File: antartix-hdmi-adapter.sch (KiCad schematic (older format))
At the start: 17 parts

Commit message: Merge PCB design - Revision bumped to 1.1.0
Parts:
- added R?: R_0R_0805, antmicro-footprints:0805-res, symbol antmicroResistorsmisc:R_0R_0805
- gave numbers to parts that had none: 17
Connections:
- net labels added: 3V3_RPI
- wire segments 144 -> 145
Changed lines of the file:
@@
 Text GLabel 1650 3575 0    50   Input ~ 0
 HDMI0_CEC
-Text GLabel 1650 3775 0    50   Input ~ 0
-VCC3V3
 Text GLabel 2900 3575 2    50   Input ~ 0
 HDMI0_SDA
@@
 	2900 3675 2525 3675
 Wire Wire Line
-	1650 3775 2025 3775
-Wire Wire Line
 	2025 3775 2025 3875
 Wire Wire Line
@@
 	2275 4150 2275 4350
 $Comp
-L power:GND #PWR?
+L power:GND #PWR09
 U 1 1 6041C11F
 P 2275 4350
-F 0 "#PWR?" H 2275 4100 50  0001 C CNN
+F 0 "#PWR09" H 2275 4100 50  0001 C CNN
 F 1 "GND" H 2280 4177 50  0000 C CNN
 F 2 "" H 2275 4350 50  0001 C CNN
@@
 $EndComp
 $Comp
-L antmicroUSBDVIHDMIConnectors:685119134923 J?
+L antmicroUSBDVIHDMIConnectors:685119134923 J8
 U 1 1 6041EE42
 P 6700 2625
-F 0 "J?" H 6700 3562 60  0000 C CNN
+F 0 "J8" H 6700 3562 60  0000 C CNN
 F 1 "685119134923" H 6700 3456 60  0000 C CNN
 F 2 "antmicro-footprints:HDMI_A_Female_685119134923" H 6900 2825 60  0001 L CNN
@@
 	6400 3425 6400 3575
 $Comp
-L power:GND #PWR?
+L power:GND #PWR028
 U 1 1 6044467C
 P 6150 3575
-F 0 "#PWR?" H 6150 3325 50  0001 C CNN
+F 0 "#PWR028" H 6150 3325 50  0001 C CNN
 F 1 "GND" H 6155 3402 50  0000 C CNN
 F 2 "" H 6150 3575 50  0001 C CNN
@@
 $EndComp
 $Comp
-L power:GND #PWR?
+L power:GND #PWR031
 U 1 1 604461F7
 P 6400 3575
-F 0 "#PWR?" H 6400 3325 50  0001 C CNN
+F 0 "#PWR031" H 6400 3325 50  0001 C CNN
 F 1 "GND" H 6405 3402 50  0000 C CNN
 F 2 "" H 6400 3575 50  0001 C CNN
@@
 $EndComp
 $Comp
-L power:GND #PWR?
+L power:GND #PWR032
 U 1 1 604480F0
 P 7275 3575
-F 0 "#PWR?" H 7275 3325 50  0001 C CNN
+F 0 "#PWR032" H 7275 3325 50  0001 C CNN
 F 1 "GND" H 7280 3402 50  0000 C CNN
 F 2 "" H 7275 3575 50  0001 C CNN
@@
 HDMI0_CK_N
 $Comp
-L antmicroTVSDiodes:TPD8S009DSMR IC?
+L antmicroTVSDiodes:TPD8S009DSMR IC2
 U 1 1 60462849
 P 7675 4825
-F 0 "IC?" H 7700 5340 50  0000 C CNN
+F 0 "IC2" H 7700 5340 50  0000 C CNN
 F 1 "TPD8S009DSMR" H 7700 5249 50  0000 C CNN
 F 2 "antmicro-footprints:R-PDSO-N15" H 9075 4475 50  0001 C CNN
@@
 $EndComp
 $Comp
-L antmicroTestPoints:TP_SMD1MM TP?
+L antmicroTestPoints:TP_SMD1MM TP1
 U 1 1 60472FDB
 P 5500 2775
-F 0 "TP?" V 5405 2822 50  0000 C CNN
+F 0 "TP1" V 5405 2822 50  0000 C CNN
 F 1 "TP_SMD1MM" H 5500 2675 50  0001 C CNN
 F 2 "antmicro-footprints:Testpoint_smd_1mm" H 5700 2975 60  0001 L CNN
@@
 $EndComp
 $Comp
-L antmicroTestPoints:TP_SMD1MM TP?
+L antmicroTestPoints:TP_SMD1MM TP2
 U 1 1 604734EB
 P 5500 2875
-F 0 "TP?" V 5405 2922 50  0000 C CNN
+F 0 "TP2" V 5405 2922 50  0000 C CNN
 F 1 "TP_SMD1MM" H 5500 2775 50  0001 C CNN
 F 2 "antmicro-footprints:Testpoint_smd_1mm" H 5700 3075 60  0001 L CNN
@@
 $EndComp
 $Comp
-L antmicroTestPoints:TP_SMD1MM TP?
+L antmicroTestPoints:TP_SMD1MM TP3
 U 1 1 604737A0
 P 5500 3075
-F 0 "TP?" V 5405 3122 50  0000 C CNN
+F 0 "TP3" V 5405 3122 50  0000 C CNN
 F 1 "TP_SMD1MM" H 5500 2975 50  0001 C CNN
 F 2 "antmicro-footprints:Testpoint_smd_1mm" H 5700 3275 60  0001 L CNN
@@
 $EndComp
 $Comp
-L antmicroTestPoints:TP_SMD1MM TP?
+L antmicroTestPoints:TP_SMD1MM TP4
 U 1 1 60474952
 P 7900 2925
-F 0 "TP?" V 7900 2875 50  0000 R CNN
+F 0 "TP4" V 7900 2875 50  0000 R CNN
 F 1 "TP_SMD1MM" H 7900 2825 50  0001 C CNN
 F 2 "antmicro-footprints:Testpoint_smd_1mm" H 8100 3125 60  0001 L CNN
@@
 $EndComp
 $Comp
-L antmicroTestPoints:TP_SMD1MM TP?
+L antmicroTestPoints:TP_SMD1MM TP5
 U 1 1 60475CA9
 P 7900 3025
-F 0 "TP?" V 7900 2975 50  0000 R CNN
+F 0 "TP5" V 7900 2975 50  0000 R CNN
 F 1 "TP_SMD1MM" H 7900 2925 50  0001 C CNN
 F 2 "antmicro-footprints:Testpoint_smd_1mm" H 8100 3225 60  0001 L CNN
@@
 HDMI0_D2_P
 $Comp
-L power:GND #PWR?
+L power:GND #PWR033
 U 1 1 604E1D01
 P 7275 5950
-F 0 "#PWR?" H 7275 5700 50  0001 C CNN
+F 0 "#PWR033" H 7275 5700 50  0001 C CNN
 F 1 "GND" H 7280 5777 50  0000 C CNN
 F 2 "" H 7275 5950 50  0001 C CNN
@@
 $EndComp
 $Comp
-L antmicroUSBDVIHDMIConnectors:685119134923 J?
+L antmicroUSBDVIHDMIConnectors:685119134923 J9
 U 1 1 604E9CC4
 P 10450 2625
-F 0 "J?" H 10450 3562 60  0000 C CNN
+F 0 "J9" H 10450 3562 60  0000 C CNN
 F 1 "685119134923" H 10450 3456 60  0000 C CNN
 F 2 "antmicro-footprints:HDMI_A_Female_685119134923" H 10650 2825 60  0001 L CNN
@@
 	10150 3425 10150 3575
 $Comp
-L power:GND #PWR?
+L power:GND #PWR034
 U 1 1 604E9CE6
 P 9900 3575
-F 0 "#PWR?" H 9900 3325 50  0001 C CNN
+F 0 "#PWR034" H 9900 3325 50  0001 C CNN
 F 1 "GND" H 9905 3402 50  0000 C CNN
 F 2 "" H 9900 3575 50  0001 C CNN
@@
 $EndComp
 $Comp
-L power:GND #PWR?
+L power:GND #PWR035
 U 1 1 604E9CEC
 P 10150 3575
-F 0 "#PWR?" H 10150 3325 50  0001 C CNN
+F 0 "#PWR035" H 10150 3325 50  0001 C CNN
 F 1 "GND" H 10155 3402 50  0000 C CNN
 F 2 "" H 10150 3575 50  0001 C CNN
@@
 $EndComp
 $Comp
-L power:GND #PWR?
+L power:GND #PWR036
 U 1 1 604E9CF2
 P 11025 3575
-F 0 "#PWR?" H 11025 3325 50  0001 C CNN
+F 0 "#PWR036" H 11025 3325 50  0001 C CNN
 F 1 "GND" H 11030 3402 50  0000 C CNN
 F 2 "" H 11025 3575 50  0001 C CNN
@@
 HDMI1_CK_N
 $Comp
-L antmicroTVSDiodes:TPD8S009DSMR IC?
+L antmicroTVSDiodes:TPD8S009DSMR IC3
 U 1 1 604E9D00
 P 11425 4825
-F 0 "IC?" H 11450 5340 50  0000 C CNN
+F 0 "IC3" H 11450 5340 50  0000 C CNN
 F 1 "TPD8S009DSMR" H 11450 5249 50  0000 C CNN
 F 2 "antmicro-footprints:R-PDSO-N15" H 12825 4475 50  0001 C CNN
@@
 $EndComp
 $Comp
-L antmicroTestPoints:TP_SMD1MM TP?
+L antmicroTestPoints:TP_SMD1MM TP6
 U 1 1 604E9D06
 P 9250 2775
-F 0 "TP?" V 9155 2822 50  0000 C CNN
+F 0 "TP6" V 9155 2822 50  0000 C CNN
 F 1 "TP_SMD1MM" H 9250 2675 50  0001 C CNN
 F 2 "antmicro-footprints:Testpoint_smd_1mm" H 9450 2975 60  0001 L CNN
@@
 $EndComp
 $Comp
-L antmicroTestPoints:TP_SMD1MM TP?
+L antmicroTestPoints:TP_SMD1MM TP7
 U 1 1 604E9D0C
 P 9250 2875
-F 0 "TP?" V 9155 2922 50  0000 C CNN
+F 0 "TP7" V 9155 2922 50  0000 C CNN
 F 1 "TP_SMD1MM" H 9250 2775 50  0001 C CNN
 F 2 "antmicro-footprints:Testpoint_smd_1mm" H 9450 3075 60  0001 L CNN
@@
 $EndComp
 $Comp
-L antmicroTestPoints:TP_SMD1MM TP?
+L antmicroTestPoints:TP_SMD1MM TP8
 U 1 1 604E9D12
 P 9250 3075
-F 0 "TP?" V 9155 3122 50  0000 C CNN
+F 0 "TP8" V 9155 3122 50  0000 C CNN
 F 1 "TP_SMD1MM" H 9250 2975 50  0001 C CNN
 F 2 "antmicro-footprints:Testpoint_smd_1mm" H 9450 3275 60  0001 L CNN
@@
 $EndComp
 $Comp
-L antmicroTestPoints:TP_SMD1MM TP?
+L antmicroTestPoints:TP_SMD1MM TP9
 U 1 1 604E9D18
 P 11650 2925
-F 0 "TP?" V 11650 2875 50  0000 R CNN
+F 0 "TP9" V 11650 2875 50  0000 R CNN
 F 1 "TP_SMD1MM" H 11650 2825 50  0001 C CNN
 F 2 "antmicro-footprints:Testpoint_smd_1mm" H 11850 3125 60  0001 L CNN
@@
 $EndComp
 $Comp
-L antmicroTestPoints:TP_SMD1MM TP?
+L antmicroTestPoints:TP_SMD1MM TP10
 U 1 1 604E9D1E
 P 11650 3025
-F 0 "TP?" V 11650 2975 50  0000 R CNN
+F 0 "TP10" V 11650 2975 50  0000 R CNN
 F 1 "TP_SMD1MM" H 11650 2925 50  0001 C CNN
 F 2 "antmicro-footprints:Testpoint_smd_1mm" H 11850 3225 60  0001 L CNN
@@
 HDMI1_D2_P
 $Comp
-L power:GND #PWR?
+L power:GND #PWR037
 U 1 1 604E9D47
 P 11025 5950
-F 0 "#PWR?" H 11025 5700 50  0001 C CNN
+F 0 "#PWR037" H 11025 5700 50  0001 C CNN
 F 1 "GND" H 11030 5777 50  0000 C CNN
 F 2 "" H 11025 5950 50  0001 C CNN
@@
 	6300 2575 5600 2575
 $Comp
-L antmicroMechanicalParts:9774030151 SP?
+L antmicroMechanicalParts:9774030151 SP1
 U 1 1 603A356D
 P 13850 2400
-F 0 "SP?" H 13980 2453 60  0000 L CNN
+F 0 "SP1" H 13980 2453 60  0000 L CNN
 F 1 "9774030151" H 13980 2347 60  0000 L CNN
 F 2 "antmicro-footprints:9774030151" H 13850 2400 60  0001 C CNN
@@
 $EndComp
 $Comp
-L antmicroMechanicalParts:9774030151 SP?
+L antmicroMechanicalParts:9774030151 SP2
 U 1 1 603A4646
 P 13850 2775
-F 0 "SP?" H 13980 2828 60  0000 L CNN
+F 0 "SP2" H 13980 2828 60  0000 L CNN
 F 1 "9774030151" H 13980 2722 60  0000 L CNN
 F 2 "antmicro-footprints:9774030151" H 13850 2775 60  0001 C CNN
@@
 $EndComp
 $Comp
-L antmicroRectangularConnectorsHeadersFemalePins:QTE-020-04-L-D-A J?
+L antmicroRectangularConnectorsHeadersFemalePins:QTE-020-04-L-D-A J7
 U 1 1 60358E48
 P 2125 1925
-F 0 "J?" H 2275 2100 50  0000 C CNN
+F 0 "J7" H 2275 2100 50  0000 C CNN
 F 1 "QTE-020-04-L-D-A" H 2275 2009 50  0000 C CNN
 F 2 "antmicro-footprints:QTE-020-04-L-D-A" H 2275 -425 60  0001 L CNN
@@
 $EndComp
 Connection ~ 2025 3775
+Text Label 1325 3775 0    50   ~ 0
+3V3_RPI
+$Comp
+L antmicroResistorsmisc:R_0R_0805 R?
+U 1 1 6051B344
+P 1175 3775
+AR Path="/6051B344" Ref="R?"  Part="1"
+AR Path="/604C47E1/6051B344" Ref="R?"  Part="1"
+F 0 "R?" H 1050 3875 60  0000 C CNN
+F 1 "R_0R_0805" H 1175 3625 60  0001 C CNN
+F 2 "antmicro-footprints:0805-res" H 1375 3975 60  0001 L CNN
+F 3 "" H 1175 3775 50  0001 C CNN
+F 4 "VISHAY" H 1375 4175 60  0001 L CNN "Manufacturer"
+F 5 "CRCW08050000Z0EA" H 1375 4075 60  0001 L CNN "MPN"
+F 6 "0R" H 1175 3875 50  0000 C CNN "Val"
+F 7 "DNP" H 1175 3775 50  0000 C CNN "Populate"
+	1    1175 3775
+	1    0    0    -1
+$EndComp
+Text Label 1325 3775 0    50   ~ 0
+3V3_RPI
+Wire Wire Line
+	1325 3775 2025 3775
+Text GLabel 950  3775 0    50   Input ~ 0
+VCC3V3
+Wire Wire Line
+	1025 3775 950  3775
 $EndSCHEMATC

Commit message: Add hierarchical structure
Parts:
- gave numbers to parts that had none: 1
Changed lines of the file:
@@
 $Descr A3 16535 11693
 encoding utf-8
-Sheet 2 2
+Sheet 2 3
 Title ""
 Date ""
@@
 	2275 4150 2275 4350
 $Comp
-L power:GND #PWR09
+L power:GND #PWR068
 U 1 1 6041C11F
 P 2275 4350
-F 0 "#PWR09" H 2275 4100 50  0001 C CNN
+AR Path="/604C47E1/6041C11F" Ref="#PWR068"  Part="1"
+AR Path="/60603DE8/6041C11F" Ref="#PWR?"  Part="1"
+F 0 "#PWR068" H 2275 4100 50  0001 C CNN
 F 1 "GND" H 2280 4177 50  0000 C CNN
 F 2 "" H 2275 4350 50  0001 C CNN
@@
 U 1 1 6041EE42
 P 6700 2625
+AR Path="/604C47E1/6041EE42" Ref="J8"  Part="1"
+AR Path="/60603DE8/6041EE42" Ref="J?"  Part="1"
 F 0 "J8" H 6700 3562 60  0000 C CNN
 F 1 "685119134923" H 6700 3456 60  0000 C CNN
@@
 	6400 3425 6400 3575
 $Comp
-L power:GND #PWR028
+L power:GND #PWR069
 U 1 1 6044467C
 P 6150 3575
-F 0 "#PWR028" H 6150 3325 50  0001 C CNN
+AR Path="/604C47E1/6044467C" Ref="#PWR069"  Part="1"
+AR Path="/60603DE8/6044467C" Ref="#PWR?"  Part="1"
+F 0 "#PWR069" H 6150 3325 50  0001 C CNN
 F 1 "GND" H 6155 3402 50  0000 C CNN
 F 2 "" H 6150 3575 50  0001 C CNN
@@
 $EndComp
 $Comp
-L power:GND #PWR031
+L power:GND #PWR070
 U 1 1 604461F7
 P 6400 3575
-F 0 "#PWR031" H 6400 3325 50  0001 C CNN
+AR Path="/604C47E1/604461F7" Ref="#PWR070"  Part="1"
+AR Path="/60603DE8/604461F7" Ref="#PWR?"  Part="1"
+F 0 "#PWR070" H 6400 3325 50  0001 C CNN
 F 1 "GND" H 6405 3402 50  0000 C CNN
 F 2 "" H 6400 3575 50  0001 C CNN
@@
 $EndComp
 $Comp
-L power:GND #PWR032
+L power:GND #PWR071
 U 1 1 604480F0
 P 7275 3575
-F 0 "#PWR032" H 7275 3325 50  0001 C CNN
+AR Path="/604C47E1/604480F0" Ref="#PWR071"  Part="1"
+AR Path="/60603DE8/604480F0" Ref="#PWR?"  Part="1"
+F 0 "#PWR071" H 7275 3325 50  0001 C CNN
 F 1 "GND" H 7280 3402 50  0000 C CNN
 F 2 "" H 7275 3575 50  0001 C CNN
@@
 U 1 1 60462849
 P 7675 4825
+AR Path="/604C47E1/60462849" Ref="IC2"  Part="1"
+AR Path="/60603DE8/60462849" Ref="IC?"  Part="1"
 F 0 "IC2" H 7700 5340 50  0000 C CNN
 F 1 "TPD8S009DSMR" H 7700 5249 50  0000 C CNN
@@
 U 1 1 60472FDB
 P 5500 2775
+AR Path="/604C47E1/60472FDB" Ref="TP1"  Part="1"
+AR Path="/60603DE8/60472FDB" Ref="TP?"  Part="1"
 F 0 "TP1" V 5405 2822 50  0000 C CNN
 F 1 "TP_SMD1MM" H 5500 2675 50  0001 C CNN
@@
 U 1 1 604734EB
 P 5500 2875
+AR Path="/604C47E1/604734EB" Ref="TP2"  Part="1"
+AR Path="/60603DE8/604734EB" Ref="TP?"  Part="1"
 F 0 "TP2" V 5405 2922 50  0000 C CNN
 F 1 "TP_SMD1MM" H 5500 2775 50  0001 C CNN
@@
 U 1 1 604737A0
 P 5500 3075
+AR Path="/604C47E1/604737A0" Ref="TP3"  Part="1"
+AR Path="/60603DE8/604737A0" Ref="TP?"  Part="1"
 F 0 "TP3" V 5405 3122 50  0000 C CNN
 F 1 "TP_SMD1MM" H 5500 2975 50  0001 C CNN
@@
 U 1 1 60474952
 P 7900 2925
+AR Path="/604C47E1/60474952" Ref="TP4"  Part="1"
+AR Path="/60603DE8/60474952" Ref="TP?"  Part="1"
 F 0 "TP4" V 7900 2875 50  0000 R CNN
 F 1 "TP_SMD1MM" H 7900 2825 50  0001 C CNN
@@
 U 1 1 60475CA9
 P 7900 3025
+AR Path="/604C47E1/60475CA9" Ref="TP5"  Part="1"
+AR Path="/60603DE8/60475CA9" Ref="TP?"  Part="1"
 F 0 "TP5" V 7900 2975 50  0000 R CNN
 F 1 "TP_SMD1MM" H 7900 2925 50  0001 C CNN
@@
 HDMI0_D2_P
 $Comp
-L power:GND #PWR033
+L power:GND #PWR072
 U 1 1 604E1D01
 P 7275 5950
-F 0 "#PWR033" H 7275 5700 50  0001 C CNN
+AR Path="/604C47E1/604E1D01" Ref="#PWR072"  Part="1"
+AR Path="/60603DE8/604E1D01" Ref="#PWR?"  Part="1"
+F 0 "#PWR072" H 7275 5700 50  0001 C CNN
 F 1 "GND" H 7280 5777 50  0000 C CNN
 F 2 "" H 7275 5950 50  0001 C CNN
@@
 U 1 1 604E9CC4
 P 10450 2625
+AR Path="/604C47E1/604E9CC4" Ref="J9"  Part="1"
+AR Path="/60603DE8/604E9CC4" Ref="J?"  Part="1"
 F 0 "J9" H 10450 3562 60  0000 C CNN
 F 1 "685119134923" H 10450 3456 60  0000 C CNN
@@
 	10150 3425 10150 3575
 $Comp
-L power:GND #PWR034
+L power:GND #PWR073
 U 1 1 604E9CE6
 P 9900 3575
-F 0 "#PWR034" H 9900 3325 50  0001 C CNN
+AR Path="/604C47E1/604E9CE6" Ref="#PWR073"  Part="1"
+AR Path="/60603DE8/604E9CE6" Ref="#PWR?"  Part="1"
+F 0 "#PWR073" H 9900 3325 50  0001 C CNN
 F 1 "GND" H 9905 3402 50  0000 C CNN
 F 2 "" H 9900 3575 50  0001 C CNN
@@
 $EndComp
 $Comp
-L power:GND #PWR035
+L power:GND #PWR074
 U 1 1 604E9CEC
 P 10150 3575
-F 0 "#PWR035" H 10150 3325 50  0001 C CNN
+AR Path="/604C47E1/604E9CEC" Ref="#PWR074"  Part="1"
+AR Path="/60603DE8/604E9CEC" Ref="#PWR?"  Part="1"
+F 0 "#PWR074" H 10150 3325 50  0001 C CNN
 F 1 "GND" H 10155 3402 50  0000 C CNN
 F 2 "" H 10150 3575 50  0001 C CNN
@@
 $EndComp
 $Comp
-L power:GND #PWR036
+L power:GND #PWR075
 U 1 1 604E9CF2
 P 11025 3575
-F 0 "#PWR036" H 11025 3325 50  0001 C CNN
+AR Path="/604C47E1/604E9CF2" Ref="#PWR075"  Part="1"
+AR Path="/60603DE8/604E9CF2" Ref="#PWR?"  Part="1"
+F 0 "#PWR075" H 11025 3325 50  0001 C CNN
 F 1 "GND" H 11030 3402 50  0000 C CNN
 F 2 "" H 11025 3575 50  0001 C CNN
@@
 U 1 1 604E9D00
 P 11425 4825
+AR Path="/604C47E1/604E9D00" Ref="IC3"  Part="1"
+AR Path="/60603DE8/604E9D00" Ref="IC?"  Part="1"
 F 0 "IC3" H 11450 5340 50  0000 C CNN
 F 1 "TPD8S009DSMR" H 11450 5249 50  0000 C CNN
@@
 U 1 1 604E9D06
 P 9250 2775
+AR Path="/604C47E1/604E9D06" Ref="TP6"  Part="1"
+AR Path="/60603DE8/604E9D06" Ref="TP?"  Part="1"
 F 0 "TP6" V 9155 2822 50  0000 C CNN
 F 1 "TP_SMD1MM" H 9250 2675 50  0001 C CNN
@@
 U 1 1 604E9D0C
 P 9250 2875
+AR Path="/604C47E1/604E9D0C" Ref="TP7"  Part="1"
+AR Path="/60603DE8/604E9D0C" Ref="TP?"  Part="1"
 F 0 "TP7" V 9155 2922 50  0000 C CNN
 F 1 "TP_SMD1MM" H 9250 2775 50  0001 C CNN
@@
 U 1 1 604E9D12
 P 9250 3075
+AR Path="/604C47E1/604E9D12" Ref="TP8"  Part="1"
+AR Path="/60603DE8/604E9D12" Ref="TP?"  Part="1"
 F 0 "TP8" V 9155 3122 50  0000 C CNN
 F 1 "TP_SMD1MM" H 9250 2975 50  0001 C CNN
@@
 U 1 1 604E9D18
 P 11650 2925
+AR Path="/604C47E1/604E9D18" Ref="TP9"  Part="1"
+AR Path="/60603DE8/604E9D18" Ref="TP?"  Part="1"
 F 0 "TP9" V 11650 2875 50  0000 R CNN
 F 1 "TP_SMD1MM" H 11650 2825 50  0001 C CNN
@@
 U 1 1 604E9D1E
 P 11650 3025
+AR Path="/604C47E1/604E9D1E" Ref="TP10"  Part="1"
+AR Path="/60603DE8/604E9D1E" Ref="TP?"  Part="1"
 F 0 "TP10" V 11650 2975 50  0000 R CNN
 F 1 "TP_SMD1MM" H 11650 2925 50  0001 C CNN
@@
 HDMI1_D2_P
 $Comp
-L power:GND #PWR037
+L power:GND #PWR076
 U 1 1 604E9D47
 P 11025 5950
-F 0 "#PWR037" H 11025 5700 50  0001 C CNN
+AR Path="/604C47E1/604E9D47" Ref="#PWR076"  Part="1"
+AR Path="/60603DE8/604E9D47" Ref="#PWR?"  Part="1"
+F 0 "#PWR076" H 11025 5700 50  0001 C CNN
 F 1 "GND" H 11030 5777 50  0000 C CNN
 F 2 "" H 11025 5950 50  0001 C CNN
@@
 U 1 1 603A356D
 P 13850 2400
+AR Path="/604C47E1/603A356D" Ref="SP1"  Part="1"
+AR Path="/60603DE8/603A356D" Ref="SP?"  Part="1"
 F 0 "SP1" H 13980 2453 60  0000 L CNN
 F 1 "9774030151" H 13980 2347 60  0000 L CNN
@@
 U 1 1 603A4646
 P 13850 2775
+AR Path="/604C47E1/603A4646" Ref="SP2"  Part="1"
+AR Path="/60603DE8/603A4646" Ref="SP?"  Part="1"
 F 0 "SP2" H 13980 2828 60  0000 L CNN
 F 1 "9774030151" H 13980 2722 60  0000 L CNN
@@
 U 1 1 60358E48
 P 2125 1925
+AR Path="/604C47E1/60358E48" Ref="J7"  Part="1"
+AR Path="/60603DE8/60358E48" Ref="J?"  Part="1"
 F 0 "J7" H 2275 2100 50  0000 C CNN
 F 1 "QTE-020-04-L-D-A" H 2275 2009 50  0000 C CNN
@@
 P 1175 3775
 AR Path="/6051B344" Ref="R?"  Part="1"
-AR Path="/604C47E1/6051B344" Ref="R?"  Part="1"
-F 0 "R?" H 1050 3875 60  0000 C CNN
+AR Path="/604C47E1/6051B344" Ref="R37"  Part="1"
+AR Path="/60603DE8/6051B344" Ref="R?"  Part="1"
+F 0 "R37" H 1050 3875 60  0000 C CNN
 F 1 "R_0R_0805" H 1175 3625 60  0001 C CNN
 F 2 "antmicro-footprints:0805-res" H 1375 3975 60  0001 L CNN

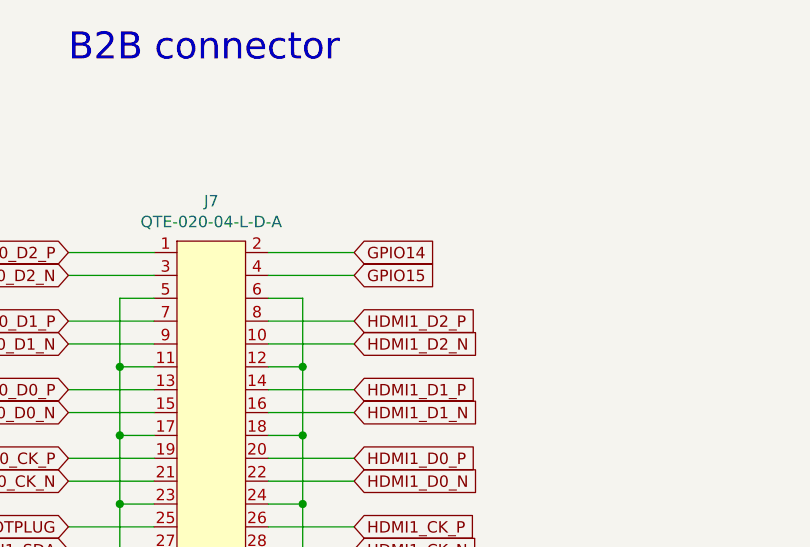
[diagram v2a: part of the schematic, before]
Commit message: Connect UART(GPIO14 & GPIO15)to BDBUS of FTDI
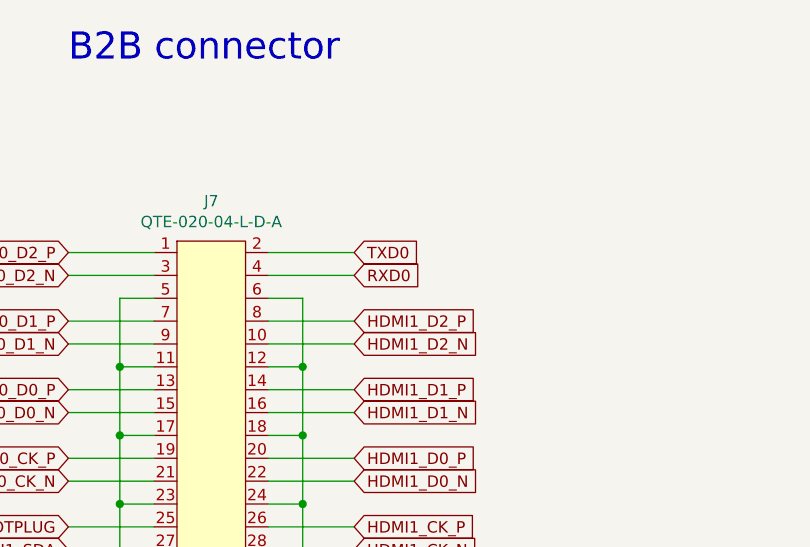
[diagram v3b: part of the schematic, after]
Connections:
- net labels added: RXD0, TXD0
- net labels removed: GPIO14, GPIO15
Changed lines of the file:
@@
 HDMI0_HOTPLUG
 Text GLabel 2900 1975 2    50   Input ~ 0
-GPIO14
+TXD0
 Text GLabel 2900 2075 2    50   Input ~ 0
-GPIO15
+RXD0
 Wire Wire Line
 	2025 1975 1650 1975

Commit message: Remove second HDMI and add LEDs to schematic
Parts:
- removed J9: 685119134923, antmicro-footprints:HDMI_A_Female_685119134923, symbol antmicroUSBDVIHDMIConnectors:685119134923
- removed TP10, TP6, TP7, TP8, TP9: TP_SMD1MM, antmicro-footprints:Testpoint_smd_1mm, symbol antmicroTestPoints:TP_SMD1MM
- added D? (x2): LG_L29K-G2J1-24-Z, antartix-arty-controller-footprints:LED_0603, symbol antartix-arty-controller:LG_L29K-G2J1-24-Z
- added R? (x2): R_470R_0402, antartix-arty-controller-footprints:0402-res, symbol antartix-arty-controller:R_470R_0402
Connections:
- wire segments 145 -> 127
- no-connect marks 2 -> 1
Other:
- note added: "TODO:Pick GPIOs for LEDS"
